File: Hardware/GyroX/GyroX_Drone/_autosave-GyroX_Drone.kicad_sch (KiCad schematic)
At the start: 55 parts, among them J1 USB_C_Receptacle_USB2.0_16P, J2 Conn_01x02, Q1 PMOS, U1 SPX3819M5-L-3-3, U2 CH340K, U3 2N7002DW, U4 TP4056-42-ESOP8, U5 MPU-6050, U6 STM32F405RGTx, U7 BMP390, U8 L86-M33

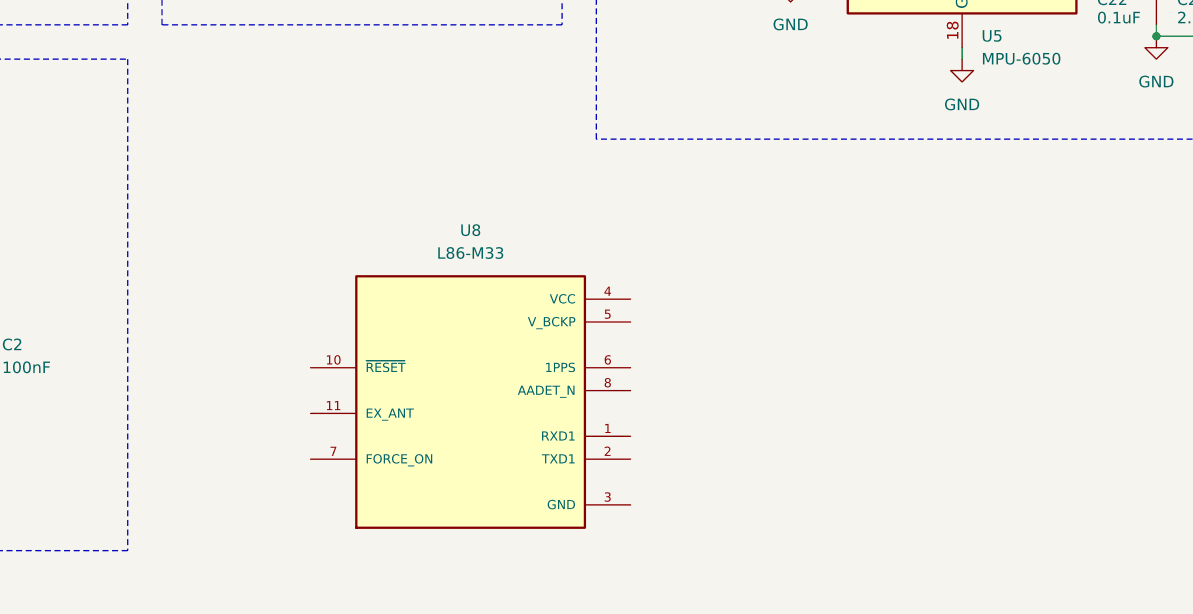
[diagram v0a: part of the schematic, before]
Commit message: GPS module designed
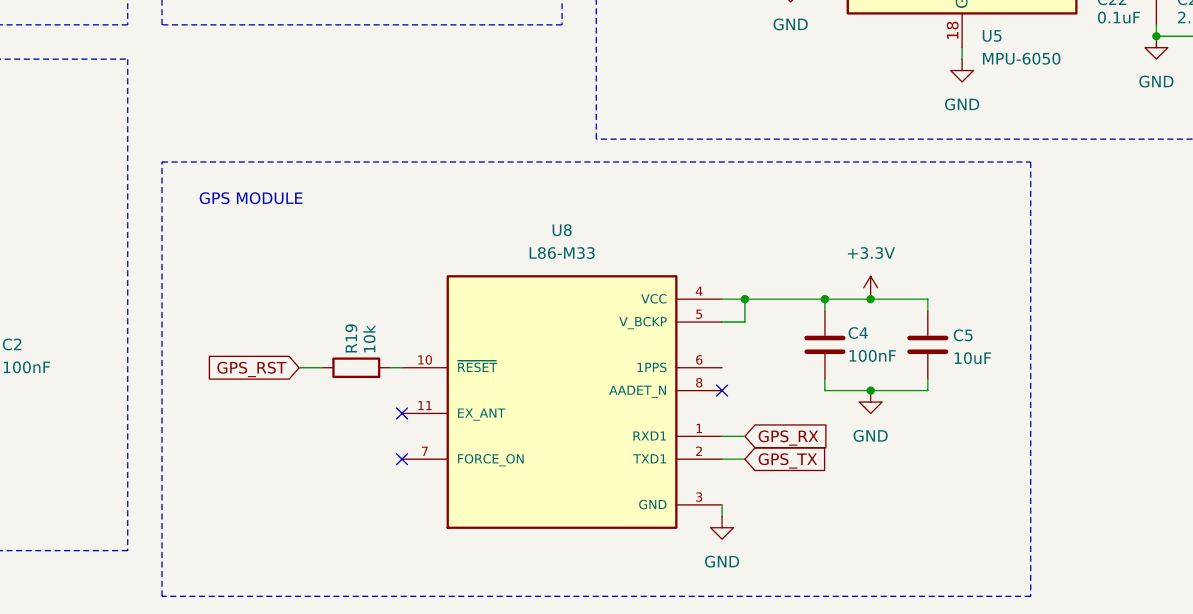
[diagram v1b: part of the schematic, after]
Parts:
- added C4: 100nF, symbol Device:C
- added C5: 10uF, symbol Device:C
- added R19: 10k, symbol Device:R
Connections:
- net +3.3V: now also U8.4 (VCC), U8.5 (V_BCKP), C4.1, C5.1
- net GND: now also U8.12 (GND), U8.3 (GND), C4.2, C5.2
- net GPS_RX: now reaches U8.1 (RXD1)
- net at U8.10 (~{RESET}): now also R19.2
- net GPS_TX: now reaches U8.2 (TXD1)
- new net GPS_RST: R19.1
- no-connect marks 3 -> 6
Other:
- note added: "GPS MODULE"
- moved on the sheet: U8

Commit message: Accelerometer added and power rail filtered
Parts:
- removed C24: 0.1uF, Capacitor_SMD:C_0603_1608Metric, symbol Device:C
- removed R15: 4.7k, symbol Device:R
- removed R16, R17, R18: 10k, symbol Device:R
- removed U5: MPU-6050, Sensor_Motion:InvenSense_QFN-24_4x4mm_P0.5mm, symbol Sensor_Motion:MPU-6050
- added FB1: FerriteBead, symbol Device:FerriteBead
- added U9: ICM-42688-P, ICM-42688-P:PQFN50P300X250X97-14N, symbol ICM-42688-P:ICM-42688-P
- C23: value 2.2nF -> 2.2uF
- C25: value 10nF -> 100nF
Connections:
- net +3.3V: now also FB1.1; no longer C2.1, C25.1, C3.1, U7.1 (VDDIO), U7.10 (VDD)
- net GND: now also C3.2, U7.3 (VSS), U9.6 (GND)
- net +3V3_SENSORS: now reaches C23.1
- net +3V3_SENSORS: now also C2.1, C22.1, C25.1, C3.1, U7.1 (VDDIO), U7.10 (VDD), FB1.2, U9.5 (VDDIO), U9.8 (VDD)
- net BMP_SCLK: now reaches U7.2 (SCK)
- net BMP_CSB: now reaches U7.6 (CSB)
- net MCU_MISO renamed BMP_MISO
- net MCU_MOSI renamed BMP_MOSI
- new net IMP_SCLK: U9.13 (AP_SCL/AP_SCLK)
- new net IMU_CS: U9.12 (AP_CS)
- new net IMU_INT: U9.4 (INT1/INT)
- new net IMU_SDI: U9.14 (AP_SDA/AP_SDIO/AP_SDI)
- new net IMU_SDO: U9.1 (AP_SDO/AP_AD0)
- no-connect marks 6 -> 8
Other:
- note added: "ACCELEROMETER + GYROSCOPE"
- note added: "DIGITAL BAROMETRIC PRESSURE SENSOR"
- note added: "GPS SENSOR"
- note removed: "GPS MODULE"
- note removed: "MPU6050 IMU"
- moved on the sheet: C19, C2, C20, C26, C27, C28, C29, C3, C30, C31, R10, R11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
